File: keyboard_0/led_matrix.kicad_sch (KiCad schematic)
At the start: 2 parts

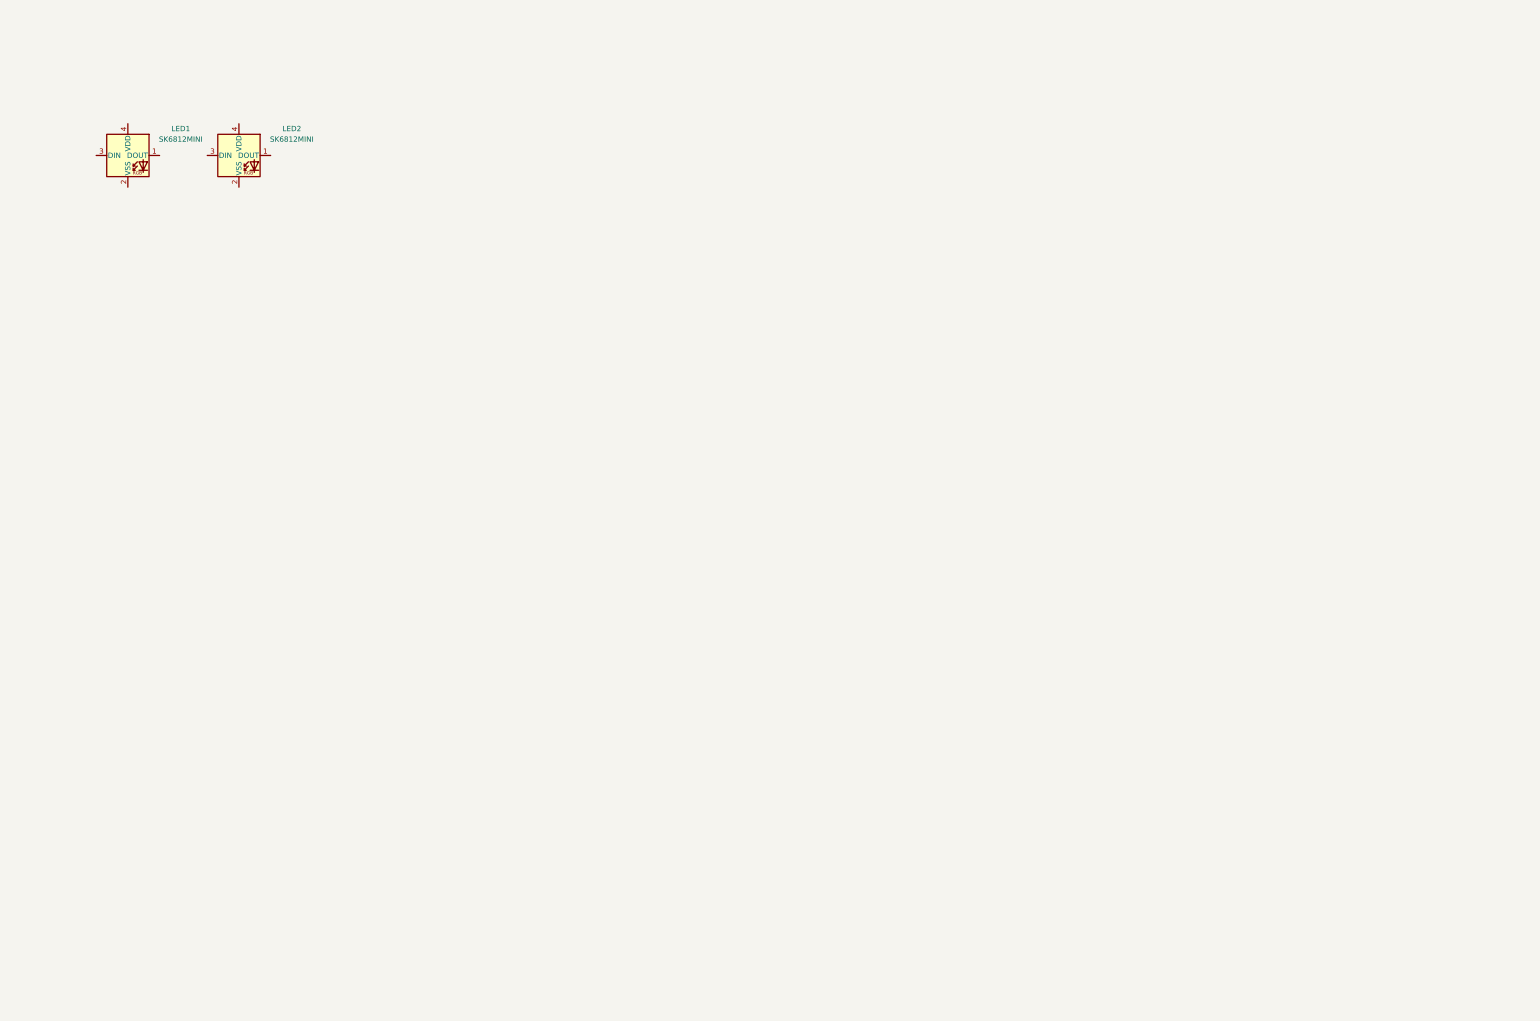
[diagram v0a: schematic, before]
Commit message: add led matrix schematic and finish adding rotary knob
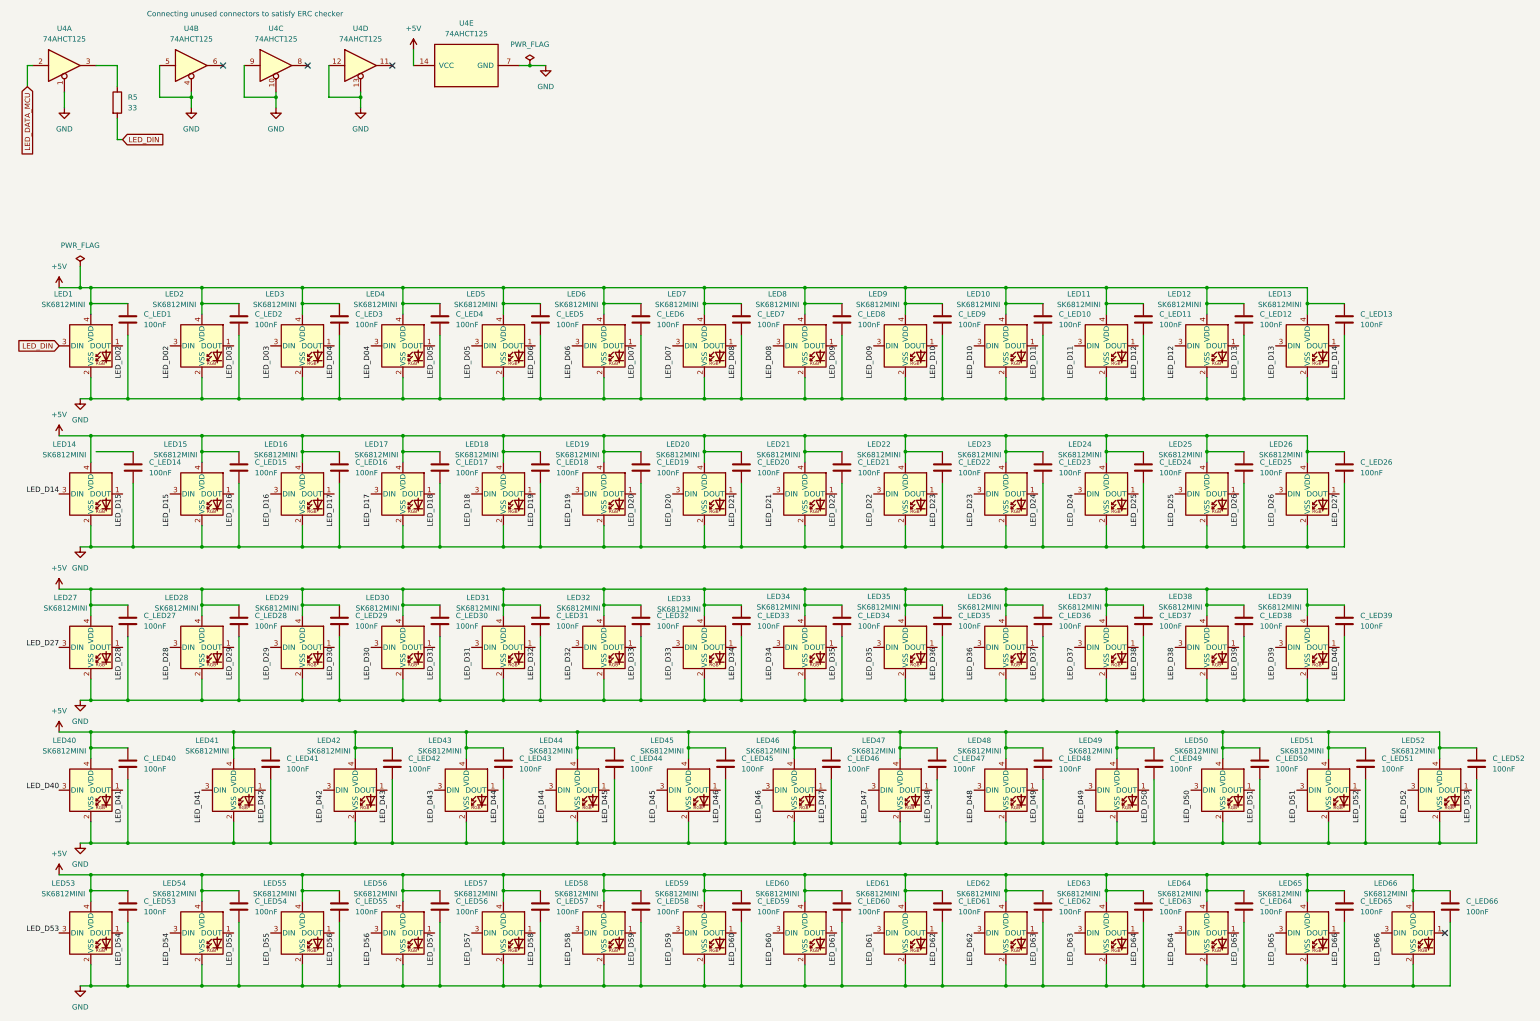
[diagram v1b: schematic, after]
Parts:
- added C_LED1, C_LED10, C_LED11, C_LED12, C_LED13, C_LED14, C_LED15, C_LED16, C_LED17, C_LED18, C_LED19, C_LED2, C_LED20, C_LED21, C_LED22, C_LED23, C_LED24, C_LED25, C_LED26, C_LED27, C_LED28, C_LED29, C_LED3, C_LED30, C_LED31, C_LED32, C_LED33, C_LED34, C_LED35, C_LED36, C_LED37, C_LED38, C_LED39, C_LED4, C_LED40, C_LED41, C_LED42, C_LED43, C_LED44, C_LED45, C_LED46, C_LED47, C_LED48, C_LED49, C_LED5, C_LED50, C_LED51, C_LED52, C_LED53, C_LED54, C_LED55, C_LED56, C_LED57, C_LED58, C_LED59, C_LED6, C_LED60, C_LED61, C_LED62, C_LED63, C_LED64, C_LED65, C_LED66, C_LED7, C_LED8, C_LED9: 100nF, Capacitor_SMD:C_0402_1005Metric, symbol Device:C
- added LED10, LED11, LED12, LED13, LED14, LED15, LED16, LED17, LED18, LED19, LED20, LED21, LED22, LED23, LED24, LED25, LED26, LED27, LED28, LED29, LED3, LED30, LED31, LED32, LED33, LED34, LED35, LED36, LED37, LED38, LED39, LED4, LED40, LED41, LED42, LED43, LED44, LED45, LED46, LED47, LED48, LED49, LED5, LED50, LED51, LED52, LED53, LED54, LED55, LED56, LED57, LED58, LED59, LED6, LED60, LED61, LED62, LED63, LED64, LED65, LED66, LED7, LED8, LED9: SK6812MINI, LED_SMD:LED_SK6812MINI_PLCC4_3.5x3.5mm_P1.75mm, symbol LED:SK6812MINI
- added R5: 33, Resistor_SMD:R_0402_1005Metric, symbol Device:R
- added U4: 74AHCT125, Package_SO:SOIC-14W_7.5x9mm_P1.27mm, symbol 74xx:74AHCT125
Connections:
- net LED_D03: now reaches LED2.1 (DOUT)
- net LED_D03: now also LED3.3 (DIN)
- net GND: now reaches LED2.2 (VSS)
- net GND: now also LED1.2 (VSS), C_LED1.2, C_LED10.2, C_LED11.2, C_LED12.2, C_LED13.2, C_LED14.2, C_LED15.2, C_LED16.2, C_LED17.2, C_LED18.2, C_LED19.2, C_LED2.2, C_LED20.2, C_LED21.2, C_LED22.2, C_LED23.2, C_LED24.2, C_LED25.2, C_LED26.2, C_LED27.2, C_LED28.2, C_LED29.2, C_LED3.2, C_LED30.2, C_LED31.2, C_LED32.2, C_LED33.2, C_LED34.2, C_LED35.2, C_LED36.2, C_LED37.2, C_LED38.2, C_LED39.2, C_LED4.2, C_LED40.2, C_LED41.2, C_LED42.2, C_LED43.2, C_LED44.2, C_LED45.2, C_LED46.2, C_LED47.2, C_LED48.2, C_LED49.2, C_LED5.2, C_LED50.2, C_LED51.2, C_LED52.2, C_LED53.2, C_LED54.2, C_LED55.2, C_LED56.2, C_LED57.2, C_LED58.2, C_LED59.2, C_LED6.2, C_LED60.2, C_LED61.2, C_LED62.2, C_LED63.2, C_LED64.2, C_LED65.2, C_LED66.2, C_LED7.2, C_LED8.2, C_LED9.2, LED10.2 (VSS), LED11.2 (VSS), LED12.2 (VSS), LED13.2 (VSS), LED14.2 (VSS), LED15.2 (VSS), LED16.2 (VSS), LED17.2 (VSS), LED18.2 (VSS), LED19.2 (VSS), LED20.2 (VSS), LED21.2 (VSS), LED22.2 (VSS), LED23.2 (VSS), LED24.2 (VSS), LED25.2 (VSS), LED26.2 (VSS), LED27.2 (VSS), LED28.2 (VSS), LED29.2 (VSS), LED3.2 (VSS), LED30.2 (VSS), LED31.2 (VSS), LED32.2 (VSS), LED33.2 (VSS), LED34.2 (VSS), LED35.2 (VSS), LED36.2 (VSS), LED37.2 (VSS), LED38.2 (VSS), LED39.2 (VSS), LED4.2 (VSS), LED40.2 (VSS), LED41.2 (VSS), LED42.2 (VSS), LED43.2 (VSS), LED44.2 (VSS), LED45.2 (VSS), LED46.2 (VSS), LED47.2 (VSS), LED48.2 (VSS), LED49.2 (VSS), LED5.2 (VSS), LED50.2 (VSS), LED51.2 (VSS), LED52.2 (VSS), LED53.2 (VSS), LED54.2 (VSS), LED55.2 (VSS), LED56.2 (VSS), LED57.2 (VSS), LED58.2 (VSS), LED59.2 (VSS), LED6.2 (VSS), LED60.2 (VSS), LED61.2 (VSS), LED62.2 (VSS), LED63.2 (VSS), LED64.2 (VSS), LED65.2 (VSS), LED66.2 (VSS), LED7.2 (VSS), LED8.2 (VSS), LED9.2 (VSS), U4.1, U4.10, U4.12, U4.13, U4.4, U4.5, U4.7 (GND), U4.9
- net LED_D02: now reaches LED2.3 (DIN)
- net LED_D02: now also LED1.1 (DOUT)
- net +5V: now reaches LED2.4 (VDD)
- net +5V: now also LED1.4 (VDD), C_LED1.1, C_LED10.1, C_LED11.1, C_LED12.1, C_LED13.1, C_LED15.1, C_LED16.1, C_LED17.1, C_LED18.1, C_LED19.1, C_LED2.1, C_LED20.1, C_LED21.1, C_LED22.1, C_LED23.1, C_LED24.1, C_LED25.1, C_LED26.1, C_LED27.1, C_LED28.1, C_LED29.1, C_LED3.1, C_LED30.1, C_LED31.1, C_LED32.1, C_LED33.1, C_LED34.1, C_LED35.1, C_LED36.1, C_LED37.1, C_LED38.1, C_LED39.1, C_LED4.1, C_LED40.1, C_LED41.1, C_LED42.1, C_LED43.1, C_LED44.1, C_LED45.1, C_LED46.1, C_LED47.1, C_LED48.1, C_LED49.1, C_LED5.1, C_LED50.1, C_LED51.1, C_LED52.1, C_LED53.1, C_LED54.1, C_LED55.1, C_LED56.1, C_LED57.1, C_LED58.1, C_LED59.1, C_LED6.1, C_LED60.1, C_LED61.1, C_LED62.1, C_LED63.1, C_LED64.1, C_LED65.1, C_LED66.1, C_LED7.1, C_LED8.1, C_LED9.1, LED10.4 (VDD), LED11.4 (VDD), LED12.4 (VDD), LED13.4 (VDD), LED14.4 (VDD), LED15.4 (VDD), LED16.4 (VDD), LED17.4 (VDD), LED18.4 (VDD), LED19.4 (VDD), LED20.4 (VDD), LED21.4 (VDD), LED22.4 (VDD), LED23.4 (VDD), LED24.4 (VDD), LED25.4 (VDD), LED26.4 (VDD), LED27.4 (VDD), LED28.4 (VDD), LED29.4 (VDD), LED3.4 (VDD), LED30.4 (VDD), LED31.4 (VDD), LED32.4 (VDD), LED33.4 (VDD), LED34.4 (VDD), LED35.4 (VDD), LED36.4 (VDD), LED37.4 (VDD), LED38.4 (VDD), LED39.4 (VDD), LED4.4 (VDD), LED40.4 (VDD), LED41.4 (VDD), LED42.4 (VDD), LED43.4 (VDD), LED44.4 (VDD), LED45.4 (VDD), LED46.4 (VDD), LED47.4 (VDD), LED48.4 (VDD), LED49.4 (VDD), LED5.4 (VDD), LED50.4 (VDD), LED51.4 (VDD), LED52.4 (VDD), LED53.4 (VDD), LED54.4 (VDD), LED55.4 (VDD), LED56.4 (VDD), LED57.4 (VDD), LED58.4 (VDD), LED59.4 (VDD), LED6.4 (VDD), LED60.4 (VDD), LED61.4 (VDD), LED62.4 (VDD), LED63.4 (VDD), LED64.4 (VDD), LED65.4 (VDD), LED66.4 (VDD), LED7.4 (VDD), LED8.4 (VDD), LED9.4 (VDD), U4.14 (VCC)
- net LED_DIN: now reaches LED1.3 (DIN)
- net LED_DIN: now also R5.2
- new net: R5.1, U4.3
- new net LED_D04: LED3.1 (DOUT), LED4.3 (DIN)
- new net LED_D05: LED4.1 (DOUT), LED5.3 (DIN)
- new net LED_D06: LED5.1 (DOUT), LED6.3 (DIN)
- new net LED_D07: LED6.1 (DOUT), LED7.3 (DIN)
- new net LED_D08: LED7.1 (DOUT), LED8.3 (DIN)
- new net LED_D09: LED8.1 (DOUT), LED9.3 (DIN)
- new net LED_D10: LED10.3 (DIN), LED9.1 (DOUT)
- new net LED_D11: LED10.1 (DOUT), LED11.3 (DIN)
- new net LED_D12: LED11.1 (DOUT), LED12.3 (DIN)
- new net LED_D13: LED12.1 (DOUT), LED13.3 (DIN)
- new net LED_D14: LED13.1 (DOUT), LED14.3 (DIN)
- new net LED_D15: LED14.1 (DOUT), LED15.3 (DIN)
- new net LED_D16: LED15.1 (DOUT), LED16.3 (DIN)
- new net LED_D17: LED16.1 (DOUT), LED17.3 (DIN)
- new net LED_D18: LED17.1 (DOUT), LED18.3 (DIN)
- new net LED_D19: LED18.1 (DOUT), LED19.3 (DIN)
- new net LED_D20: LED19.1 (DOUT), LED20.3 (DIN)
- new net LED_D21: LED20.1 (DOUT), LED21.3 (DIN)
- new net LED_D22: LED21.1 (DOUT), LED22.3 (DIN)
- new net LED_D23: LED22.1 (DOUT), LED23.3 (DIN)
- new net LED_D24: LED23.1 (DOUT), LED24.3 (DIN)
- new net LED_D25: LED24.1 (DOUT), LED25.3 (DIN)
- new net LED_D26: LED25.1 (DOUT), LED26.3 (DIN)
- new net LED_D27: LED26.1 (DOUT), LED27.3 (DIN)
- new net LED_D28: LED27.1 (DOUT), LED28.3 (DIN)
- new net LED_D29: LED28.1 (DOUT), LED29.3 (DIN)
- new net LED_D30: LED29.1 (DOUT), LED30.3 (DIN)
- new net LED_D31: LED30.1 (DOUT), LED31.3 (DIN)
- new net LED_D32: LED31.1 (DOUT), LED32.3 (DIN)
- new net LED_D33: LED32.1 (DOUT), LED33.3 (DIN)
- new net LED_D34: LED33.1 (DOUT), LED34.3 (DIN)
- new net LED_D35: LED34.1 (DOUT), LED35.3 (DIN)
- new net LED_D36: LED35.1 (DOUT), LED36.3 (DIN)
- new net LED_D37: LED36.1 (DOUT), LED37.3 (DIN)
- new net LED_D38: LED37.1 (DOUT), LED38.3 (DIN)
- new net LED_D39: LED38.1 (DOUT), LED39.3 (DIN)
- new net LED_D40: LED39.1 (DOUT), LED40.3 (DIN)
- new net LED_D41: LED40.1 (DOUT), LED41.3 (DIN)
- new net LED_D42: LED41.1 (DOUT), LED42.3 (DIN)
- new net LED_D43: LED42.1 (DOUT), LED43.3 (DIN)
- new net LED_D44: LED43.1 (DOUT), LED44.3 (DIN)
- new net LED_D45: LED44.1 (DOUT), LED45.3 (DIN)
- new net LED_D46: LED45.1 (DOUT), LED46.3 (DIN)
- new net LED_D47: LED46.1 (DOUT), LED47.3 (DIN)
- new net LED_D48: LED47.1 (DOUT), LED48.3 (DIN)
- new net LED_D49: LED48.1 (DOUT), LED49.3 (DIN)
- new net LED_D50: LED49.1 (DOUT), LED50.3 (DIN)
- new net LED_D51: LED50.1 (DOUT), LED51.3 (DIN)
- new net LED_D52: LED51.1 (DOUT), LED52.3 (DIN)
- new net LED_D53: LED52.1 (DOUT), LED53.3 (DIN)
- new net LED_D54: LED53.1 (DOUT), LED54.3 (DIN)
- new net LED_D55: LED54.1 (DOUT), LED55.3 (DIN)
- new net LED_D56: LED55.1 (DOUT), LED56.3 (DIN)
- new net LED_D57: LED56.1 (DOUT), LED57.3 (DIN)
- new net LED_D58: LED57.1 (DOUT), LED58.3 (DIN)
- new net LED_D59: LED58.1 (DOUT), LED59.3 (DIN)
- new net LED_D60: LED59.1 (DOUT), LED60.3 (DIN)
- new net LED_D61: LED60.1 (DOUT), LED61.3 (DIN)
- new net LED_D62: LED61.1 (DOUT), LED62.3 (DIN)
- new net LED_D63: LED62.1 (DOUT), LED63.3 (DIN)
- new net LED_D64: LED63.1 (DOUT), LED64.3 (DIN)
- new net LED_D65: LED64.1 (DOUT), LED65.3 (DIN)
- new net LED_D66: LED65.1 (DOUT), LED66.3 (DIN)
- new net LED_DATA_MCU: U4.2
- no-connect marks 0 -> 4
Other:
- note added: "Connecting unused connectors to satisfy ERC checker"
- moved on the sheet: LED1, LED2
